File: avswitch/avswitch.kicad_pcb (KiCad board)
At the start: 4 copper layers, 208 x 116 mm, 265 parts, among them J401 694106301002, J402 Screw_Terminal_01x03, J504 MUX, J701 CTRL, J703 Conn_01x02, J704 Conn_01x04, U401 TPS561243DRLR, U402 LM2611xMF, U501 RS8754, U502 RS8754, U503 RS8754, U504 RS8754, U505 RS8754, U506 RS8754, U507 74HC4052D, U508 74HC4052D, U509 74HC4052D, U601 RS8754, U602 RS8754

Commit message: PCB Layout nearing completion
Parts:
- removed C422, C423, C425, C427: 22uF, Capacitor_SMD:C_1210_3225Metric
- removed J401: 694106301002, Connector_BarrelJack:BarrelJack_Wuerth_6941xx301002
- removed R409: 0.324, Resistor_SMD:R_0805_2012Metric
- removed the REF** at (209.5, 81.0)
- removed the REF** at (225.0, 120.5)
- removed the REF** at (114.0, 131.0)
- removed the REF** at (114.0, 88.5)
- added C435: 0.1uF, Capacitor_SMD:C_0402_1005Metric, F.Cu at (259.5, 113.5)
- added C436: 10uF, Capacitor_SMD:C_1210_3225Metric, F.Cu at (255.5, 110.0)
- added D501: D_TVS_Filled, Diode_SMD:D_SOD-323, F.Cu at (105.5, 74.5)
- added D502: D_TVS_Filled, Diode_SMD:D_SOD-323, F.Cu at (109.5, 52.0)
- added D503: D_TVS_Filled, Diode_SMD:D_SOD-323, F.Cu at (103.0, 49.5)
- added D504: D_TVS_Filled, Diode_SMD:D_SOD-323, F.Cu at (101.5, 74.5)
- added D505: D_TVS_Filled, Diode_SMD:D_SOD-323, F.Cu at (88.0, 73.0)
- added D506: D_TVS_Filled, Diode_SMD:D_SOD-323, F.Cu at (82.0, 70.5)
- added D507: D_TVS_Filled, Diode_SMD:D_SOD-323, F.Cu at (151.0, 67.5)
- added D508: D_TVS_Filled, Diode_SMD:D_SOD-323, F.Cu at (155.0, 45.0)
- added D509: D_TVS_Filled, Diode_SMD:D_SOD-323, F.Cu at (142.5, 45.0)
- added D510: D_TVS_Filled, Diode_SMD:D_SOD-323, F.Cu at (147.0, 67.5)
- added D511: D_TVS_Filled, Diode_SMD:D_SOD-323, F.Cu at (131.0, 45.0)
- added D512: D_TVS_Filled, Diode_SMD:D_SOD-323, F.Cu at (118.0, 45.0)
- added D513: D_TVS_Filled, Diode_SMD:D_SOD-323, F.Cu at (200.5, 67.5)
- added D514: D_TVS_Filled, Diode_SMD:D_SOD-323, F.Cu at (204.5, 45.0)
- added D515: D_TVS_Filled, Diode_SMD:D_SOD-323, F.Cu at (192.5, 45.0)
- added D516: D_TVS_Filled, Diode_SMD:D_SOD-323, F.Cu at (196.4, 67.5)
- added D517: D_TVS_Filled, Diode_SMD:D_SOD-323, F.Cu at (179.5, 45.0)
- added D518: D_TVS_Filled, Diode_SMD:D_SOD-323, F.Cu at (167.5, 45.0)
- added D601: D_TVS_Filled, Diode_SMD:D_SOD-323, F.Cu at (251.9, 93.5)
- added D602: D_TVS_Filled, Diode_SMD:D_SOD-323, F.Cu at (246.5, 73.0)
- added D603: D_TVS_Filled, Diode_SMD:D_SOD-323, F.Cu at (242.6, 73.0)
- added D604: D_TVS_Filled, Diode_SMD:D_SOD-323, F.Cu at (237.0, 93.5)
- added D605: D_TVS_Filled, Diode_SMD:D_SOD-323, F.Cu at (225.5, 51.5)
- added D606: D_TVS_Filled, Diode_SMD:D_SOD-323, F.Cu at (218.5, 51.5)
- added J403: SamySky UJC-H-G-SMT-2-P6-TR, Connector_USB:USB_C_Receptacle_GCT_USB4125-xx-x_6P_TopMnt_Horizontal, F.Cu at (248.5, 56.0)
- added R413: 5.1k, Resistor_SMD:R_0805_2012Metric, F.Cu at (251.0, 106.0)
- added R416: 10k, Resistor_SMD:R_0805_2012Metric, F.Cu at (263.5, 110.1)
- added REF**: MountingHole_3.2mm_M3_Pad_TopBottom, MountingHole:MountingHole_3.2mm_M3_Pad_TopBottom, F.Cu at (236.5, 109.5)
- added REF**: MountingHole_3.2mm_M3_Pad_TopBottom, MountingHole:MountingHole_3.2mm_M3_Pad_TopBottom, F.Cu at (185.0, 70.0)
- added REF**: MountingHole_3.2mm_M3_Pad_TopBottom, MountingHole:MountingHole_3.2mm_M3_Pad_TopBottom, F.Cu at (125.0, 70.0)
- added REF**: MountingHole_3.2mm_M3_Pad_TopBottom, MountingHole:MountingHole_3.2mm_M3_Pad_TopBottom, F.Cu at (110.0, 115.0)
- added U403: SRV05-4, Package_TO_SOT_SMD:SOT-23-6, F.Cu at (250.5, 110.0)
- added U404: AP22816BKEWT, Package_TO_SOT_SMD:SOT-23-5, F.Cu at (260.0, 110.0)
- C406: value 470uF -> 100uF; footprint Capacitor_THT:CP_Radial_D8.0mm_P3.50mm -> Capacitor_THT:CP_Radial_D6.3mm_P2.50mm
- R411: value 0.681 -> 5.1k
- moved R408 313.3 mm to (65.0, 133.0), turned to 180 degrees
- moved C429 305.5 mm to (67.0, 110.5), turned to 90 degrees
- moved C428 302.8 mm to (70.5, 110.5), turned to 90 degrees
- moved C426 302.2 mm to (67.0, 115.5), turned to -90 degrees
- moved C424 296.2 mm to (70.5, 115.5), turned to -90 degrees
- moved R410 295.7 mm to (73.5, 111.0), turned to 90 degrees
- moved R403 290.7 mm to (65.0, 135.5)
- moved C404 286.6 mm to (65.0, 139.5), turned to -90 degrees
- moved R404 284.3 mm to (81.5, 110.0)
- moved U401 282.4 mm to (68.3, 133.0), turned to 180 degrees
- moved C416 280.4 mm to (69.0, 131.0)
- moved C414 279.3 mm to (71.0, 134.0)
- moved R406 277.9 mm to (85.5, 107.0), turned to 180 degrees
- moved C408 277.4 mm to (85.0, 134.5), turned to -90 degrees
- moved C417 277.0 mm to (86.0, 112.0), turned to 180 degrees
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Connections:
- net Net-(CONN501A-BL) renamed RCA_Y_1
- net Net-(CONN501A-TL) renamed RCA_Pb_1
- net Net-(CONN501B-BC) renamed RCA_Comp_1
- net Net-(CONN501B-TC) renamed RCA_Pr_1
- net Net-(CONN501C-BR) renamed RCA_Left_1
- net Net-(CONN501C-TR) renamed RCA_Right_1
- net Net-(CONN502A-BL) renamed RCA_Y_2
- net Net-(CONN502A-TL) renamed RCA_Pb_2
- net Net-(CONN502B-BC) renamed RCA_Comp_2
- net Net-(CONN502B-TC) renamed RCA_Pr_2
- net Net-(CONN502C-BR) renamed RCA_Left_2
- net Net-(CONN502C-TR) renamed RCA_Right_2
- net Net-(CONN503A-BL) renamed RCA_Y_3
- net Net-(CONN503A-TL) renamed RCA_Pb_3
- net Net-(CONN503B-BC) renamed RCA_Comp_3
- net Net-(CONN503B-TC) renamed RCA_Pr_3
- net Net-(CONN503C-BR) renamed RCA_Left_3
- net Net-(CONN503C-TR) renamed RCA_Right_3
- net Net-(CONN601A-BL) renamed RCA_Y_Out
- net Net-(CONN601A-TL) renamed RCA_Pb_Out
- net Net-(CONN601B-BC) renamed RCA_Comp_Out
- net Net-(CONN601B-TC) renamed RCA_Pr_Out
- net Net-(CONN601C-BR) renamed RCA_Left_Out
- net Net-(CONN601C-TR) renamed RCA_Right_Out
- A701 pad 10: unconnected-(A701-D7-Pad10) -> SEL_INPUT2
- A701 pad 11: SEL_INPUT3 -> SEL_INPUT0
- A701 pad 12: SEL_INPUT2 -> SEL_INPUT3
- A701 pad 14: SEL_INPUT0 -> ~{EN_MUX0}
- A701 pad 16: ~{EN_MUX0} -> unconnected-(A701-D13-Pad16)
- A701 pad 19: unconnected-(A701-A0-Pad19) -> AUTO_DET_Y
- A701 pad 20: unconnected-(A701-A1-Pad20) -> AUTO_DET_COMP
- A701 pad 21: BTN -> CC2
- A701 pad 22: unconnected-(A701-A3-Pad22) -> CC1
- A701 pad 25: AUTO_DET_COMP -> unconnected-(A701-A6-Pad25)
- A701 pad 26: AUTO_DET_Y -> BTN
- F401 pad 2: +5V -> VBUS
- J402 pad 1: +2V5 -> -2V5
- J402 pad 4: -2V5 -> +2V5
- R411 pad 1: Net-(C419-Pad1) -> CC1
- R411 pad 2: Net-(C422-Pad1) -> GND
- R701 pad 2: SEL_INPUT3 -> SEL_INPUT2
- R702 pad 2: SEL_INPUT2 -> SEL_INPUT0
- R703 pad 2: SEL_INPUT1 -> SEL_INPUT3
- R704 pad 2: SEL_INPUT0 -> SEL_INPUT1
- R705 pad 2: ~{EN_MUX1} -> ~{EN_MUX0}
- R706 pad 2: ~{EN_MUX0} -> ~{EN_MUX1}
- U507 pad 1: /Switch/Y1 -> /Switch/Y3
- U507 pad 12: /Switch/Pb1 -> /Switch/Pb3
- U507 pad 15: /Switch/Pb3 -> /Switch/Pb1
- U507 pad 2: /Switch/Y3 -> /Switch/Y2
- U507 pad 4: /Switch/Y4 -> /Switch/Y1
- U507 pad 5: /Switch/Y2 -> /Switch/Y4
- U508 pad 1: /Switch/Comp1 -> /Switch/Comp3
- U508 pad 12: /Switch/Pr1 -> /Switch/Pr3
- U508 pad 15: /Switch/Pr3 -> /Switch/Pr1
- U508 pad 2: /Switch/Comp3 -> /Switch/Comp2
- U508 pad 4: /Switch/Comp4 -> /Switch/Comp1
- U508 pad 5: /Switch/Comp2 -> /Switch/Comp4
- U509 pad 1: /Switch/Left1 -> /Switch/Left3
- U509 pad 2: /Switch/Left3 -> /Switch/Left2
- U509 pad 4: /Switch/Left4 -> /Switch/Left1
- U509 pad 5: /Switch/Left2 -> /Switch/Left4
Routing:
- net -2V5: track 3.02 -> 366.2 mm, vias 0 -> 12
- net CC1: track 0.00 -> 162.6 mm, vias 0 -> 1
- net CC2: track 0.00 -> 161.1 mm, vias 0 -> 1
- net /Switch/Pr1: track 0.00 -> 157.0 mm, vias 0 -> 2
- net SEL_INPUT0: track 0.00 -> 156.0 mm, vias 0 -> 5
- net /Switch/Y1: track 0.00 -> 150.7 mm, vias 0 -> 2
- net /Switch/Left1: track 0.00 -> 142.4 mm, vias 0 -> 2
- net /Switch/Pb1: track 0.00 -> 141.2 mm, vias 0 -> 2
- net /Switch/Comp1: track 0.00 -> 139.0 mm, vias 0 -> 2
- net /Switch/Right1: track 0.00 -> 137.9 mm
- net ~{EN_MUX0}: track 0.00 -> 131.1 mm, vias 0 -> 4
- net SEL_INPUT1: track 0.00 -> 130.3 mm, vias 0 -> 5
- net /Switch/Pr2: track 0.00 -> 124.2 mm, vias 0 -> 2
- net /Switch/Left2: track 0.00 -> 122.7 mm, vias 0 -> 2
- net /Switch/Right2: track 0.00 -> 118.7 mm, vias 0 -> 2
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- added copper zone on In2.Cu, net +2V5
- added copper zone on In2.Cu, net +5V
- added copper zone on F.Cu, net -2V5
- added copper zone on In2.Cu, net -2V5
- added copper zone on B.Cu, net GND
- added copper zone on F.Cu, net GND
- added copper zone on In1.Cu, net GND
- added copper zone on F.Cu, net Net-(C424-Pad1)
- added copper zone on In2.Cu, net VBUS
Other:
- outline, holes or cut-outs redrawn
- board text added: "+2V5"
- board text added: "-2V5"

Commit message: V0.1 ordered from jlpcb
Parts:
- C417: value 1uF -> 1.0uF
- CONN501, CONN502, CONN503, CONN601: value ~ -> SameSky RCJ-61562423
- J403: value SamySky UJC-H-G-SMT-2-P6-TR -> SameSky UJC-H-G-SMT-2-P6-TR
- R507, R508, R509, R510, R511, R512, R525, R526, R527, R528, R529, R530, R552, R553, R554, R561, R562, R563, R601, R602, R603, R622, R623, R624, R633, R634: value 10K -> 10k
- R607, R608, R609, R616, R617, R618, R626, R630: value 549 -> 499
- R701, R702, R703, R704, R705, R706, R707, R708, R710: value 4.7K -> 4.7k
- moved REF** 24.6 mm to (247.5, 131.5)
- moved R403 2.50 mm to (63.0, 134.0), turned to 90 degrees
- moved D605 1.95 mm to (223.6, 51.5)
- moved C418 1.50 mm to (83.5, 108.0)
- moved R408 1.12 mm to (65.5, 134.0), turned to -90 degrees
- moved F401 0.71 mm to (244.0, 62.0)
- moved J402 0.50 mm to (103.5, 140.0)
- moved R404 0.50 mm to (82.0, 110.0)
- moved R406 0.50 mm to (86.0, 107.0), turned to 90 degrees
- moved R623 0.09 mm to (237.5, 84.5)
- moved R511 0.09 mm to (147.5, 48.0)
- turned C521 to 0 degrees
- turned R564 to 0 degrees
- turned R504 to 0 degrees
- turned R551 to 0 degrees
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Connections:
- J701 pad 10: GND -> AUTO_DET_Y
- J701 pad 12: GND -> AUTO_DET_COMP
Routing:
- net GND: track 52.8 -> 147.2 mm, vias 26 -> 95
- net AUTO_DET_COMP: track 115.1 -> 148.9 mm
- net AUTO_DET_Y: track 95.6 -> 128.4 mm
- net +2V5: track 46.5 -> 77.0 mm, vias 7 -> 17
- net Net-(U501A-+INA): track 0.00 -> 10.0 mm
- net Net-(U501D-+IND): track 0.00 -> 9.89 mm
- net Net-(U503D-+IND): track 0.00 -> 9.80 mm
- net Net-(U503A-+INA): track 0.00 -> 9.80 mm
- net Net-(U505D-+IND): track 0.00 -> 9.79 mm
- net Net-(U501C-+INC): track 0.00 -> 9.78 mm
- net Net-(U505A-+INA): track 0.00 -> 9.77 mm
- net Net-(U504D-+IND): track 0.00 -> 9.75 mm
- net Net-(U506A-+INA): track 0.00 -> 9.74 mm
- net Net-(U503B-+INB): track 0.00 -> 9.74 mm
- net Net-(U506D-+IND): track 0.00 -> 9.74 mm
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- added copper zone on F.Cu, net +2V5
- added copper zone on F.Cu, net +5V
- added copper zone on F.Cu, net Net-(C405-Pad1)
- added copper zone on F.Cu, net Net-(C408-Pad1)
- added copper zone on F.Cu, net Net-(C419-Pad1)
- added copper zone on F.Cu, net Net-(C431-Pad1)
- added copper zone on F.Cu, net Net-(D401-A)
- added copper zone on F.Cu, net Net-(R404-Pad2)
- added copper zone on F.Cu, net Net-(U401-BST)
- added copper zone on F.Cu, net Net-(U401-FB)
- added copper zone on F.Cu, net Net-(U401-SW)
- added copper zone on F.Cu, net Net-(U401-VIN)
- added copper zone on F.Cu, net Net-(U402-NFB)
- added copper zone on F.Cu, net Net-(U402-SW)
- added copper zone on F.Cu, net Net-(U402-VIN)
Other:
- board text added: "(C) 2025 Michael McMaster https://github.com/mmcmaster-au/avswitch Version 0.1"
- board text added: "JLPCB 2d Barcode 10*10mm"

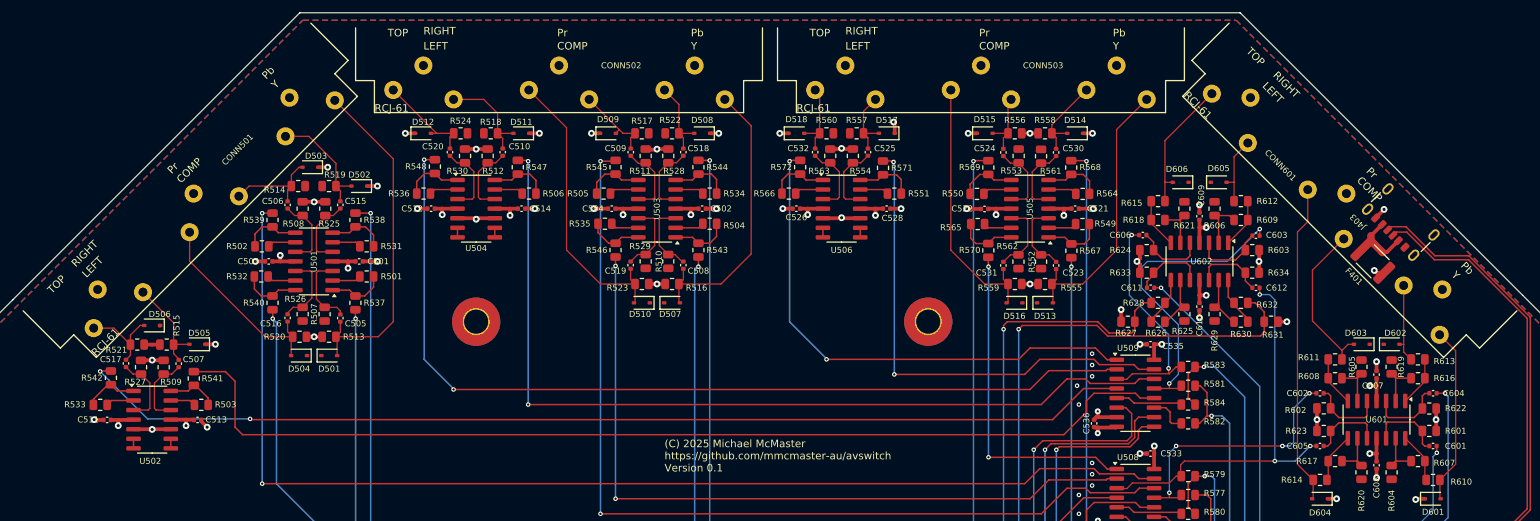
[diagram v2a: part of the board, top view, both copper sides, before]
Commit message: v2 pcb - fix up RCA footprint, screw terminal bom
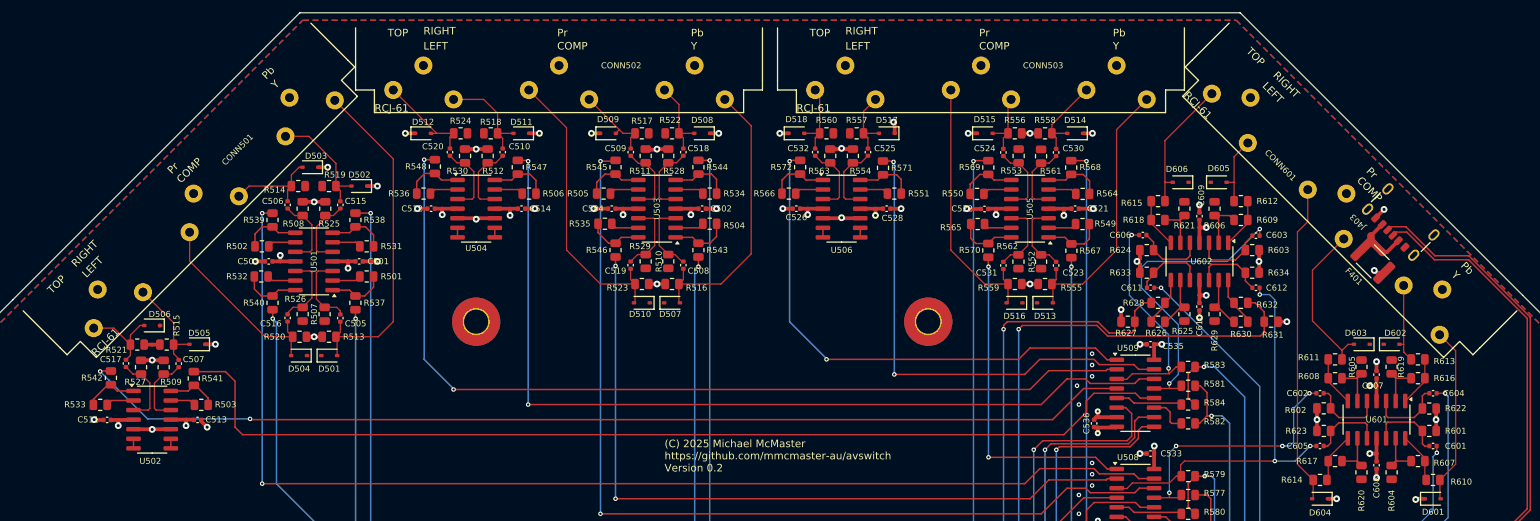
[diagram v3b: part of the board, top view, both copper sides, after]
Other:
- board text added: "(C) 2025 Michael McMaster https://github.com/mmcmaster-au/avswitch Version 0.2"
- board text removed: "(C) 2025 Michael McMaster https://github.com/mmcmaster-au/avswitch Version 0.1"
